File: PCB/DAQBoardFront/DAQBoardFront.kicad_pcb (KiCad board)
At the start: 2 copper layers, 94 x 68 mm, 4 parts, among them J2 53375-0410

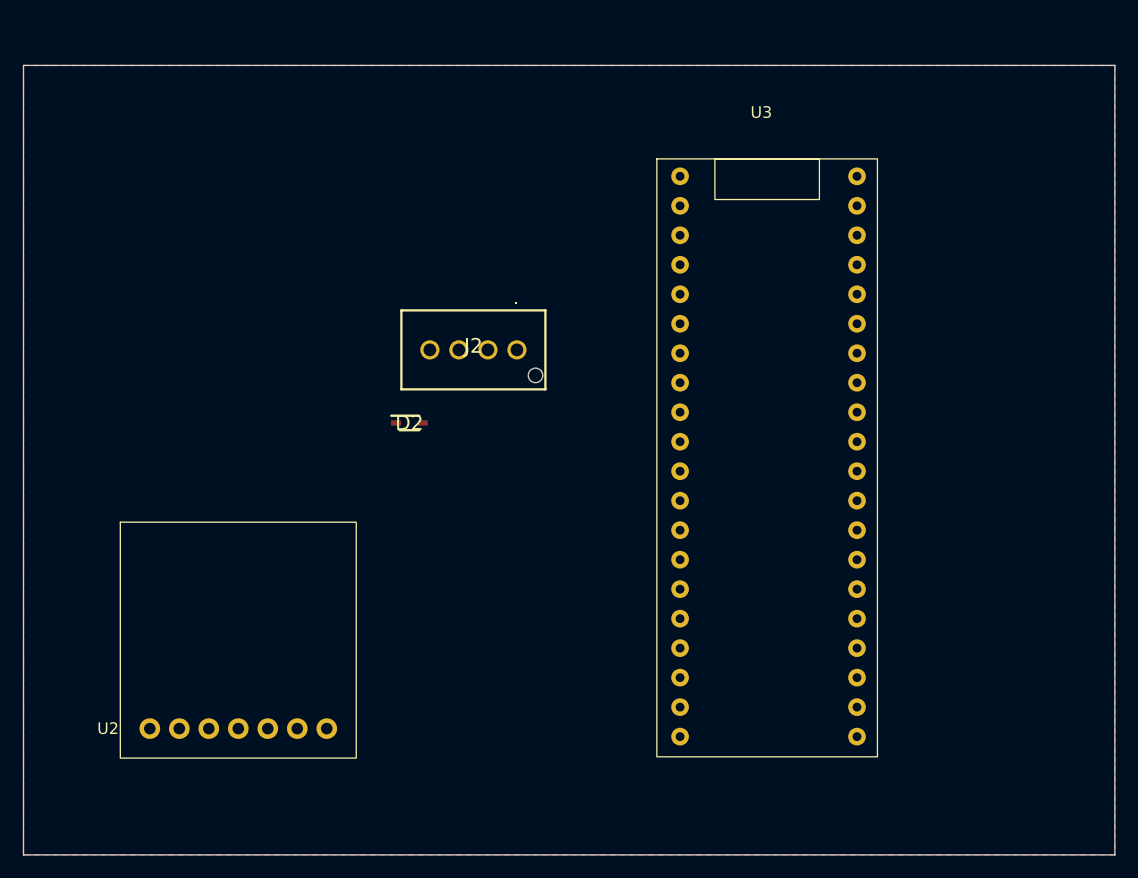
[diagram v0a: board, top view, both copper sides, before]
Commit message: Added more footprints/symbols for 8-pin input and SMD components
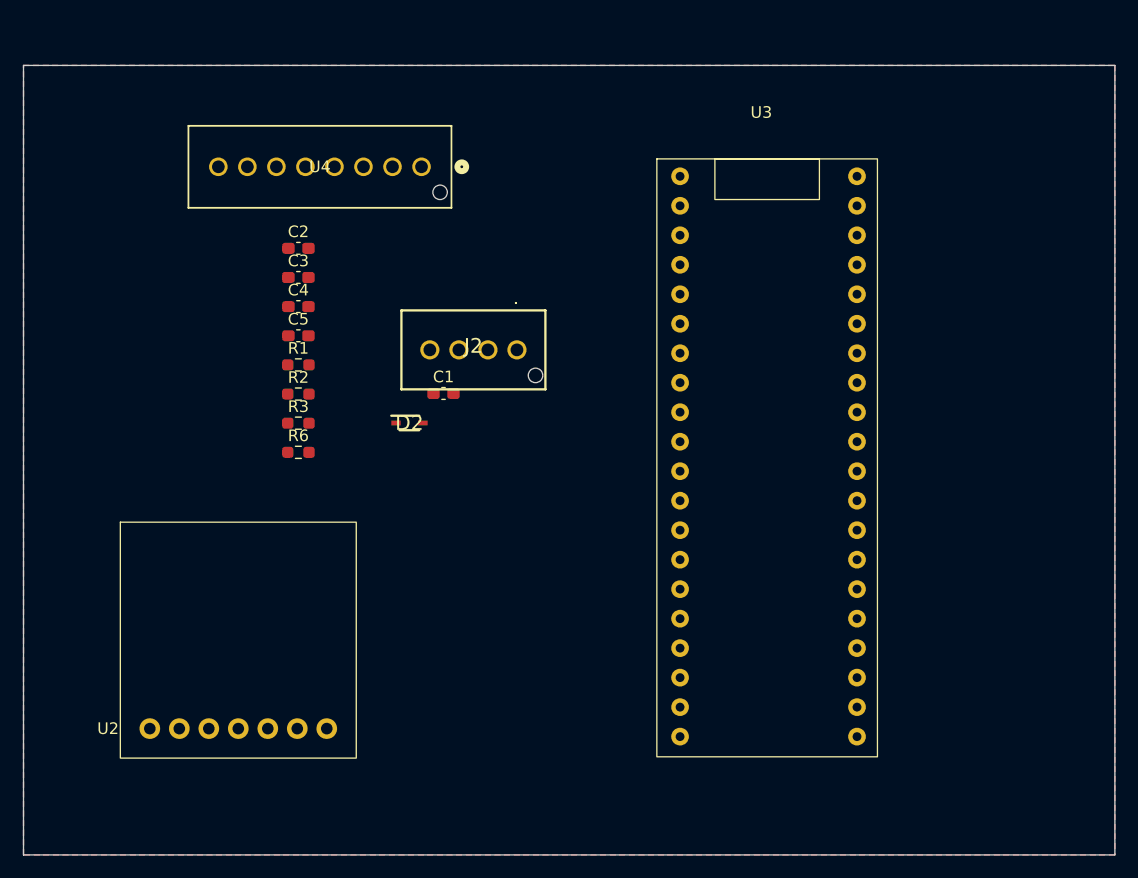
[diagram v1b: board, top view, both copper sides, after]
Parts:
- added C1: C, Capacitor_SMD:C_0603_1608Metric_Pad1.08x0.95mm_HandSolder, F.Cu at (134.7, 91.8)
- added C2: 1u, Capacitor_SMD:C_0603_1608Metric_Pad1.08x0.95mm_HandSolder, F.Cu at (122.2, 79.3)
- added C3: 1u, Capacitor_SMD:C_0603_1608Metric_Pad1.08x0.95mm_HandSolder, F.Cu at (122.2, 81.8)
- added C4: C, Capacitor_SMD:C_0603_1608Metric_Pad1.08x0.95mm_HandSolder, F.Cu at (122.2, 84.3)
- added C5: C, Capacitor_SMD:C_0603_1608Metric_Pad1.08x0.95mm_HandSolder, F.Cu at (122.2, 86.8)
- added R1: 1.69k, Resistor_SMD:R_0603_1608Metric_Pad0.98x0.95mm_HandSolder, F.Cu at (122.2, 89.3)
- added R2: 1.69k, Resistor_SMD:R_0603_1608Metric_Pad0.98x0.95mm_HandSolder, F.Cu at (122.2, 91.8)
- added R3: R, Resistor_SMD:R_0603_1608Metric_Pad0.98x0.95mm_HandSolder, F.Cu at (122.2, 94.3)
- added R6: R, Resistor_SMD:R_0603_1608Metric_Pad0.98x0.95mm_HandSolder, F.Cu at (122.2, 96.8)
- added U4: ~, CFR-Footprint-Library:CONN08_533750810_MOL, F.Cu at (132.8, 72.2)
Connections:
- U3 pad 32: /ExtraDigital3 -> /ExtraDigital
- U3 pad 33: /ExtraDigital2 -> /FRHallEffect
- U3 pad 34: /ExtraDigital1 -> /FLHallEffect
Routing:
- added copper zone on B.Cu, net /GND

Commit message: Version 1.0 completed
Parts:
- added L1: 10u, Inductor_SMD:L_0805_2012Metric_Pad1.05x1.20mm_HandSolder, B.Cu at (155.2, 113.3)
- added L2: 10u, Inductor_SMD:L_0805_2012Metric_Pad1.05x1.20mm_HandSolder, B.Cu at (158.2, 110.8)
- added L3: L, Inductor_SMD:L_0805_2012Metric_Pad1.05x1.20mm_HandSolder, B.Cu at (161.2, 108.3)
- added R4: 24k, LED_SMD:LED_0603_1608Metric_Pad1.05x0.95mm_HandSolder, B.Cu at (152.9, 76.0)
- added R5: 2k, Resistor_SMD:R_0603_1608Metric_Pad0.98x0.95mm_HandSolder, B.Cu at (152.8, 82.2)
- added U1: ~, CFR-Footprint-Library:MODULE_2019, F.Cu at (119.8, 116.8)
- C1, C2, C3, C4, C5, D2, R1, R2, R3, R6: moved to B.Cu
- moved U4 57.7 mm to (104.0, 122.2), turned to -90 degrees
- moved U2 53.1 mm to (104.0, 67.8), turned to -90 degrees
- moved R6 42.3 mm to (164.2, 101.6), turned to -90 degrees
- moved C5 41.8 mm to (162.5, 97.8), turned to -90 degrees
- moved C2 40.7 mm to (153.5, 105.3), turned to -90 degrees
- moved C4 40.6 mm to (159.5, 100.3), turned to -90 degrees
- moved C3 40.2 mm to (156.5, 102.8), turned to -90 degrees
- moved R3 40.2 mm to (161.2, 104.1), turned to -90 degrees
- moved R2 39.0 mm to (158.2, 106.6), turned to -90 degrees
- moved R1 38.5 mm to (155.2, 109.1), turned to -90 degrees
- moved J2 37.1 mm to (104.0, 90.0), turned to 90 degrees
- moved D2 27.0 mm to (154.0, 79.1), turned to 180 degrees
- moved C1 24.0 mm to (110.7, 92.3), turned to 90 degrees
- moved U3 22.1 mm to (134.0, 66.4)
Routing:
- net /ExtraAnalog: track 0.00 -> 74.3 mm
- net /SteeringAngle: track 0.00 -> 63.7 mm
- net /Brake P Input: track 0.00 -> 63.5 mm, vias 0 -> 1
- net /FLSus: track 0.00 -> 58.4 mm
- net /FLHallEffect: track 0.00 -> 55.9 mm
- net /FRHallEffect: track 0.00 -> 55.8 mm
- net /ExtraDigital: track 0.00 -> 55.8 mm
- net /FRSus: track 0.00 -> 53.8 mm
- net /CANTx: track 0.00 -> 35.7 mm
- net /CANRx: track 0.00 -> 33.6 mm
- net Net-(U3-A3): track 0.00 -> 17.7 mm
- net /Acc SCL: track 0.00 -> 16.6 mm
- net Net-(U3-A2): track 0.00 -> 14.7 mm
- net /+3.3V: track 0.00 -> 13.7 mm
- net /CAN Hi: track 0.00 -> 13.4 mm
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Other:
- board size 94 x 68 mm -> 69.8 x 64.2 mm

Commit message: DAQ board moving towards multi-voltage level architecture & custom CAN module, WIP
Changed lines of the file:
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@@
 			(outputformat 1)
 			(mirror no)
-			(drillshape 1)
+			(drillshape 0)
 			(scaleselection 1)
-			(outputdirectory "")
+			(outputdirectory "outputs/")
 		)
 	)
@@
 		(at 134.01 66.4)
 		(property "Reference" "U3"
-			(at 7 -5.5 0)
+			(at 7.64 3.7 0)
 			(unlocked yes)
 			(layer "F.SilkS")
@@
 		)
 		(property "Value" "~"
-			(at 7 -4 0)
+			(at 7.64 5.2 0)
 			(unlocked yes)
 			(layer "F.Fab")
@@
 		)
 		(fp_text user "${REFERENCE}"
-			(at 7 -2.5 0)
+			(at 7.64 6.7 0)
 			(unlocked yes)
 			(layer "F.Fab")
@@
 		(at 119.75 116.75 180)
 		(property "Reference" "U1"
-			(at -7.235 -10.635 0)
+			(at -11.9 -6.75 0)
 			(layer "F.SilkS")
 			(effects
@@
 	)
 	(segment
-		(start 106.25 97.6125)
-		(end 104.1125 97.6125)
-		(width 0.2)
-		(layer "B.Cu")
-		(net "/+3.3V")
-	)
-	(segment
-		(start 152.9 75.125)
-		(end 152.895 75.125)
-		(width 0.2)
-		(layer "B.Cu")
-		(net "/+3.3V")
-	)
-	(segment
-		(start 110.7 93.1625)
-		(end 106.25 97.6125)
+		(start 125.25 75.42)
+		(end 134.01 84.18)
 		(width 0.2)
 		(layer "B.Cu")
-		(net "/+3.3V")
+		(net "/CANRx")
 	)
 	(segment
-		(start 104.1125 97.6125)
-		(end 104 97.5)
+		(start 104 75.42)
+		(end 125.25 75.42)
 		(width 0.2)
 		(layer "B.Cu")
-		(net "/+3.3V")
+		(net "/CANRx")
 	)
 	(segment
-		(start 152.895 75.125)
-		(end 149.25 71.48)
+		(start 104 72.88)
+		(end 120.17 72.88)
 		(width 0.2)
-		(layer "B.Cu")
-		(net "/+3.3V")
+		(layer "F.Cu")
+		(net "/CANTx")
 	)
 	(segment
-		(start 148.675 98.15)
-		(end 149.825 98.15)
+		(start 120.17 72.88)
+		(end 134.01 86.72)
 		(width 0.2)
-		(layer "B.Cu")
-		(net "/GND")
+		(layer "F.Cu")
+		(net "/CANTx")
 	)
 	(segment
-		(start 148.675 103.25)
-		(end 149.825 103.25)
+		(start 131.83 99.42)
+		(end 134.01 99.42)
 		(width 0.2)
-		(layer "B.Cu")
-		(net "/GND")
+		(layer "F.Cu")
+		(net "/Acc SCL")
 	)
 	(segment
-		(start 148.65 100.7)
-		(end 149.8 100.7)
+		(start 123.56 110.4)
+		(end 123.56 107.69)
 		(width 0.2)
-		(layer "B.Cu")
-		(net "/GND")
+		(layer "F.Cu")
+		(net "/Acc SCL")
 	)
 	(segment
-		(start 149.25 101.96)
-		(end 156.4325 101.96)
+		(start 123.56 107.69)
+		(end 131.83 99.42)
 		(width 0.2)
-		(layer "B.Cu")
-		(net "Net-(U3-A1)")
+		(layer "F.Cu")
+		(net "/Acc SCL")
 	)
 	(segment
-		(start 156.4325 101.96)
-		(end 156.46 101.9875)
+		(start 131.54 101.96)
+		(end 134.01 101.96)
 		(width 0.2)
-		(layer "B.Cu")
-		(net "Net-(U3-A1)")
+		(layer "F.Cu")
+		(net "/Acc SDA")
 	)
 	(segment
-		(start 156.46 101.9875)
-		(end 158.21 103.7375)
+		(start 126.1 110.4)
+		(end 126.1 107.4)
 		(width 0.2)
-		(layer "B.Cu")
-		(net "Net-(U3-A1)")
+		(layer "F.Cu")
+		(net "/Acc SDA")
 	)
 	(segment
-		(start 158.21 103.7375)
-		(end 158.21 105.6875)
+		(start 126.1 107.4)
+		(end 131.54 101.96)
 		(width 0.2)
-		(layer "B.Cu")
-		(net "Net-(U3-A1)")
+		(layer "F.Cu")
+		(net "/Acc SDA")
 	)
 	(segment
@@
 	)
 	(segment
-		(start 155.21 112.2)
-		(end 155.21 110.0125)
+		(start 149.25 101.96)
+		(end 156.4325 101.96)
 		(width 0.2)
 		(layer "B.Cu")
-		(net "Net-(L1-Pad1)")
+		(net "Net-(U3-A1)")
+	)
+	(segment
+		(start 156.4325 101.96)
+		(end 156.46 101.9875)
+		(width 0.2)
+		(layer "B.Cu")
+		(net "Net-(U3-A1)")
+	)
+	(segment
+		(start 156.46 101.9875)
+		(end 158.21 103.7375)
+		(width 0.2)
+		(layer "B.Cu")
+		(net "Net-(U3-A1)")
+	)
+	(segment
+		(start 158.21 103.7375)
+		(end 158.21 105.6875)
+		(width 0.2)
+		(layer "B.Cu")
+		(net "Net-(U3-A1)")
 	)
 	(segment
@@
 	)
 	(segment
-		(start 125.25 75.42)
-		(end 134.01 84.18)
-		(width 0.2)
-		(layer "B.Cu")
-		(net "/CANRx")
-	)
-	(segment
-		(start 104 75.42)
-		(end 125.25 75.42)
-		(width 0.2)
-		(layer "B.Cu")
-		(net "/CANRx")
-	)
-	(segment
-		(start 104 72.88)
-		(end 120.17 72.88)
-		(width 0.2)
-		(layer "F.Cu")
-		(net "/CANTx")
-	)
-	(segment
-		(start 120.17 72.88)
-		(end 134.01 86.72)
-		(width 0.2)
-		(layer "F.Cu")
-		(net "/CANTx")
-	)
-	(segment
-		(start 131.83 99.42)
-		(end 134.01 99.42)
-		(width 0.2)
-		(layer "F.Cu")
-		(net "/Acc SCL")
-	)
-	(segment
-		(start 123.56 110.4)
-		(end 123.56 107.69)
-		(width 0.2)
-		(layer "F.Cu")
-		(net "/Acc SCL")
-	)
-	(segment
-		(start 123.56 107.69)
-		(end 131.83 99.42)
-		(width 0.2)
-		(layer "F.Cu")
-		(net "/Acc SCL")
-	)
-	(segment
-		(start 131.54 101.96)
-		(end 134.01 101.96)
-		(width 0.2)
-		(layer "F.Cu")
-		(net "/Acc SDA")
-	)
-	(segment
-		(start 126.1 110.4)
-		(end 126.1 107.4)
-		(width 0.2)
-		(layer "F.Cu")
-		(net "/Acc SDA")
-	)
-	(segment
-		(start 126.1 107.4)
-		(end 131.54 101.96)
-		(width 0.2)
-		(layer "F.Cu")
-		(net "/Acc SDA")
-	)
-	(segment
 		(start 149.25 86.72)
 		(end 140.37 95.6)
@@
 	)
 	(segment
+		(start 106.25 97.6125)
+		(end 104.1125 97.6125)
+		(width 0.2)
+		(layer "B.Cu")
+		(net "/+3.3V")
+	)
+	(segment
+		(start 152.9 75.125)
+		(end 152.895 75.125)
+		(width 0.2)
+		(layer "B.Cu")
+		(net "/+3.3V")
+	)
+	(segment
+		(start 110.7 93.1625)
+		(end 106.25 97.6125)
+		(width 0.2)
+		(layer "B.Cu")
+		(net "/+3.3V")
+	)
+	(segment
+		(start 104.1125 97.6125)
+		(end 104 97.5)
+		(width 0.2)
+		(layer "B.Cu")
+		(net "/+3.3V")
+	)
+	(segment
+		(start 152.895 75.125)
+		(end 149.25 71.48)
+		(width 0.2)
+		(layer "B.Cu")
+		(net "/+3.3V")
+	)
+	(segment
+		(start 148.675 98.15)
+		(end 149.825 98.15)
+		(width 0.2)
+		(layer "B.Cu")
+		(net "/GND")
+	)
+	(segment
+		(start 148.675 103.25)
+		(end 149.825 103.25)
+		(width 0.2)
+		(layer "B.Cu")
+		(net "/GND")
+	)
+	(segment
+		(start 148.65 100.7)
+		(end 149.8 100.7)
+		(width 0.2)
+		(layer "B.Cu")
+		(net "/GND")
+	)
+	(segment
 		(start 102.25 82.25)
 		(end 102.25 90.75)
@@
 	)
 	(segment
-		(start 161.21 107.2)
-		(end 161.21 105.0125)
+		(start 158.21 107.5125)
+		(end 158.21 109.7)
 		(width 0.2)
 		(layer "B.Cu")
-		(net "Net-(L3-Pad1)")
+		(net "Net-(L2-Pad1)")
 	)
 	(segment
-		(start 158.21 107.5125)
-		(end 158.21 109.7)
+		(start 155.21 112.2)
+		(end 155.21 110.0125)
 		(width 0.2)
 		(layer "B.Cu")
-		(net "Net-(L2-Pad1)")
+		(net "Net-(L1-Pad1)")
+	)
+	(segment
+		(start 161.21 107.2)
+		(end 161.21 105.0125)
+		(width 0.2)
+		(layer "B.Cu")
+		(net "Net-(L3-Pad1)")
 	)
 	(zone

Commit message: Slightly restructured dashboard, updated daq board schematic with buck converter and can module
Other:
- board text added: "Need to figure out pinout of common-mode choke"
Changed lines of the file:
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@@
 		(layer "Edge.Cuts")
+	)
+	(gr_text "Need to figure out pinout of common-mode choke"
+		(at 87.15 61.4 0)
+		(layer "Cmts.User")
+		(effects
+			(font
+				(size 1 1)
+				(thickness 0.15)
+			)
+			(justify left bottom)
+		)
 	)
 	(segment

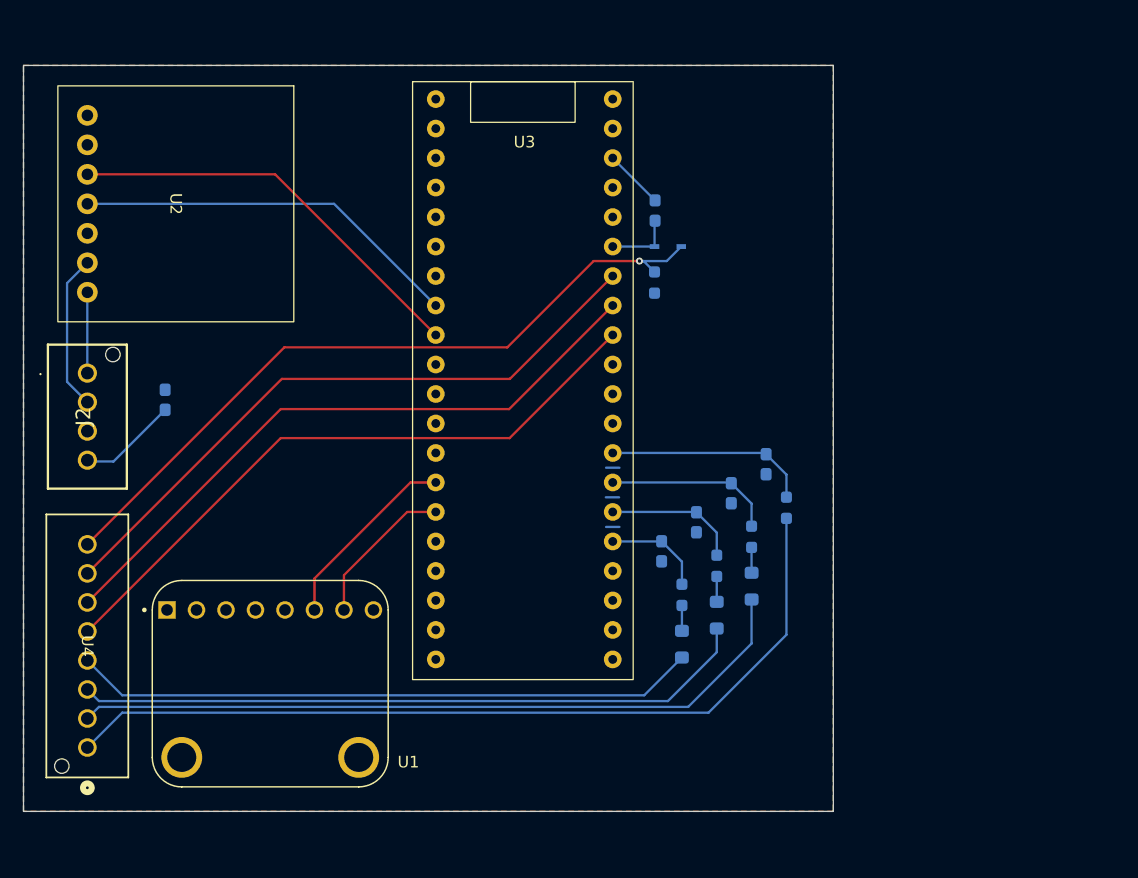
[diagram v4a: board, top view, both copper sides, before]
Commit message: Sized buck converter traces, began re-routing DAQ board
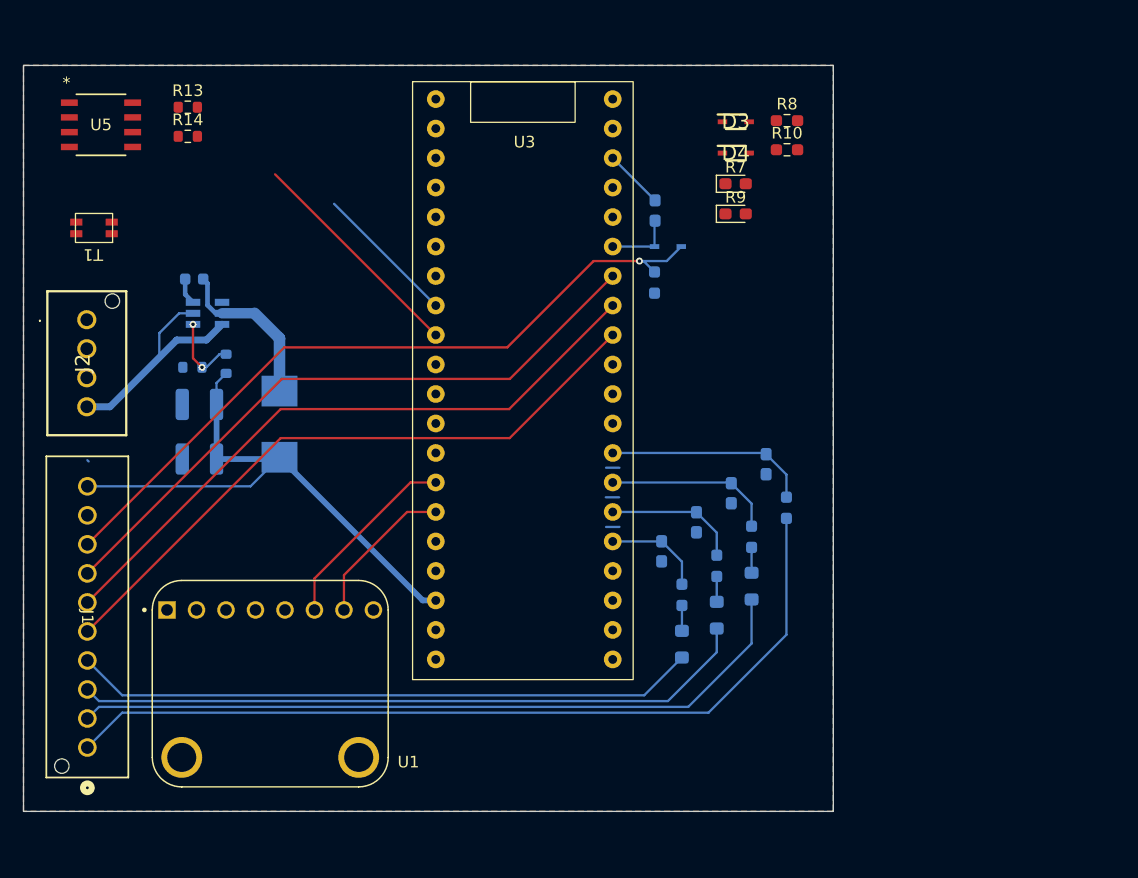
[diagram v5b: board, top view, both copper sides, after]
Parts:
- removed U2: ~, CFR-Footprint-Library:Adafruit CAN Pal
- removed U4: ~, CFR-Footprint-Library:CONN08_533750810_MOL
- added C6: CL32A226KOJNNNE, Capacitor_SMD:C_1210_3225Metric, B.Cu at (113.7, 92.7)
- added C7: CL32A226KOJNNNE, Capacitor_SMD:C_1210_3225Metric, B.Cu at (113.7, 97.4)
- added D3: 1N4148WS, CFR-Footprint-Library:SODFL2512X90N, F.Cu at (159.8, 68.3)
- added D4: 1N4148WS, CFR-Footprint-Library:SODFL2512X90N, F.Cu at (159.8, 71.0)
- added IC2: LMR51430YDDCR, CFR-Footprint-Library:SOT95P280X110-6N, B.Cu at (114.3, 84.8)
- added J1: ~, CFR-Footprint-Library:CONN10_533751010_MOL, F.Cu at (104.0, 122.2)
- added L4: PA4341.682ANLT, CFR-Footprint-Library:INDPM7166X300N, B.Cu at (120.5, 94.4)
- added R10: 2k, Resistor_SMD:R_0603_1608Metric_Pad0.98x0.95mm_HandSolder, F.Cu at (164.3, 70.8)
- added R11: ERA-3AED104V, Resistor_SMD:R_0603_1608Metric, B.Cu at (116.0, 89.2)
- added R12: ERJ-3EKF1372V, Resistor_SMD:R_0603_1608Metric, B.Cu at (113.0, 89.5)
- added R13: 60, Resistor_SMD:R_0603_1608Metric, F.Cu at (112.7, 67.1)
- added R14: 60, Resistor_SMD:R_0603_1608Metric, F.Cu at (112.7, 69.6)
- added R7: 24k, LED_SMD:LED_0603_1608Metric_Pad1.05x0.95mm_HandSolder, F.Cu at (159.8, 73.7)
- added R8: 2k, Resistor_SMD:R_0603_1608Metric_Pad0.98x0.95mm_HandSolder, F.Cu at (164.3, 68.3)
- added R9: 24k, LED_SMD:LED_0603_1608Metric_Pad1.05x0.95mm_HandSolder, F.Cu at (159.8, 76.3)
- added T1: AC1210-110-C, CFR-Footprint-Library:AC1210-110-C, F.Cu at (106.1, 78.0)
- added U5: TCAN1051VDRQ1, CFR-Footprint-Library:D8_TEX, F.Cu at (105.2, 68.6)
- C1: value C -> CC0603KRX7R7BB104; footprint Capacitor_SMD:C_0603_1608Metric_Pad1.08x0.95mm_HandSolder -> Capacitor_SMD:C_0603_1608Metric
- moved C1 10.7 mm to (113.2, 81.9), turned to 0 degrees
- moved J2 4.60 mm to (104.0, 85.4)
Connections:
- net /Brake P Input renamed /Brake P Input (12V)
- C1 pad 1: /+3.3V -> Net-(IC2-CB)
- C1 pad 2: /GND -> Net-(IC2-SW)
- J2 pad 4: /+3.3V -> /+12V
- U3 pad 18: unconnected-(U3-5V-Pad18) -> +5V
- U3 pad 19: unconnected-(U3-G-Pad19) -> /GND
- U3 pad 33: /FRHallEffect -> Net-(D4-A)
- U3 pad 34: /FLHallEffect -> Net-(D3-A)
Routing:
- net +5V: track 0.00 -> 49.4 mm
- net /CANRx: track 33.6 -> 12.4 mm
- net /+12V: track 0.00 -> 20.5 mm
- net /CANTx: track 35.7 -> 19.6 mm
- net Net-(IC2-SW): track 0.00 -> 14.3 mm
- net /CAN Hi: track 13.4 -> 0.00 mm
- net /+3.3V: track 13.7 -> 5.16 mm
- net /CAN Lo: track 6.96 -> 0.00 mm
- net Net-(IC2-FB): track 0.00 -> 6.81 mm, vias 0 -> 2
- net Net-(IC2-CB): track 0.00 -> 2.28 mm
- added copper zone on F.Cu, net /GND
- removed copper zone on F.Cu, net /+3.3V
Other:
- board text added: "BUCK 12V->5V"
